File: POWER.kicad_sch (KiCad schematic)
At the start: 39 parts, among them CN1 KF128L-5.08-2P, U1 XL1509-5.0, U2 B0503S-2WR3L, U3 SY8089A1AAC, U4 CH213K, U5 SY8089AAC

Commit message: 更新PCB层叠铺铜与器件封装配置
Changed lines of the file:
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@@
 	)
 	(junction
-		(at 241.3 137.16)
+		(at 238.125 137.16)
 		(diameter 0)
 		(color 0 0 0 0)
@@
 	(wire
 		(pts
-			(xy 226.06 137.16) (xy 241.3 137.16)
+			(xy 226.06 137.16) (xy 238.125 137.16)
 		)
 		(stroke
@@
 	(wire
 		(pts
-			(xy 241.3 137.16) (xy 252.73 137.16)
+			(xy 238.125 137.16) (xy 252.73 137.16)
 		)
 		(stroke
@@
 	(symbol
 		(lib_id "power:Earth")
-		(at 241.3 137.16 0)
+		(at 238.125 137.16 0)
 		(unit 1)
 		(body_style 1)
@@
 		(fields_autoplaced yes)
 		(property "Reference" "#PWR027"
-			(at 241.3 143.51 0)
+			(at 238.125 143.51 0)
 			(hide yes)
 			(show_name no)
@@
 		)
 		(property "Value" "Earth"
-			(at 241.3 142.24 0)
+			(at 238.125 142.24 0)
 			(show_name no)
 			(do_not_autoplace no)
@@
 		)
 		(property "Footprint" ""
-			(at 241.3 137.16 0)
+			(at 238.125 137.16 0)
 			(hide yes)
 			(show_name no)
@@
 		)
 		(property "Datasheet" ""
-			(at 241.3 137.16 0)
+			(at 238.125 137.16 0)
 			(hide yes)
 			(show_name no)
@@
 		)
 		(property "Description" "Power symbol creates a global label with name \"Earth\""
-			(at 241.3 137.16 0)
+			(at 238.125 137.16 0)
 			(hide yes)
 			(show_name no)

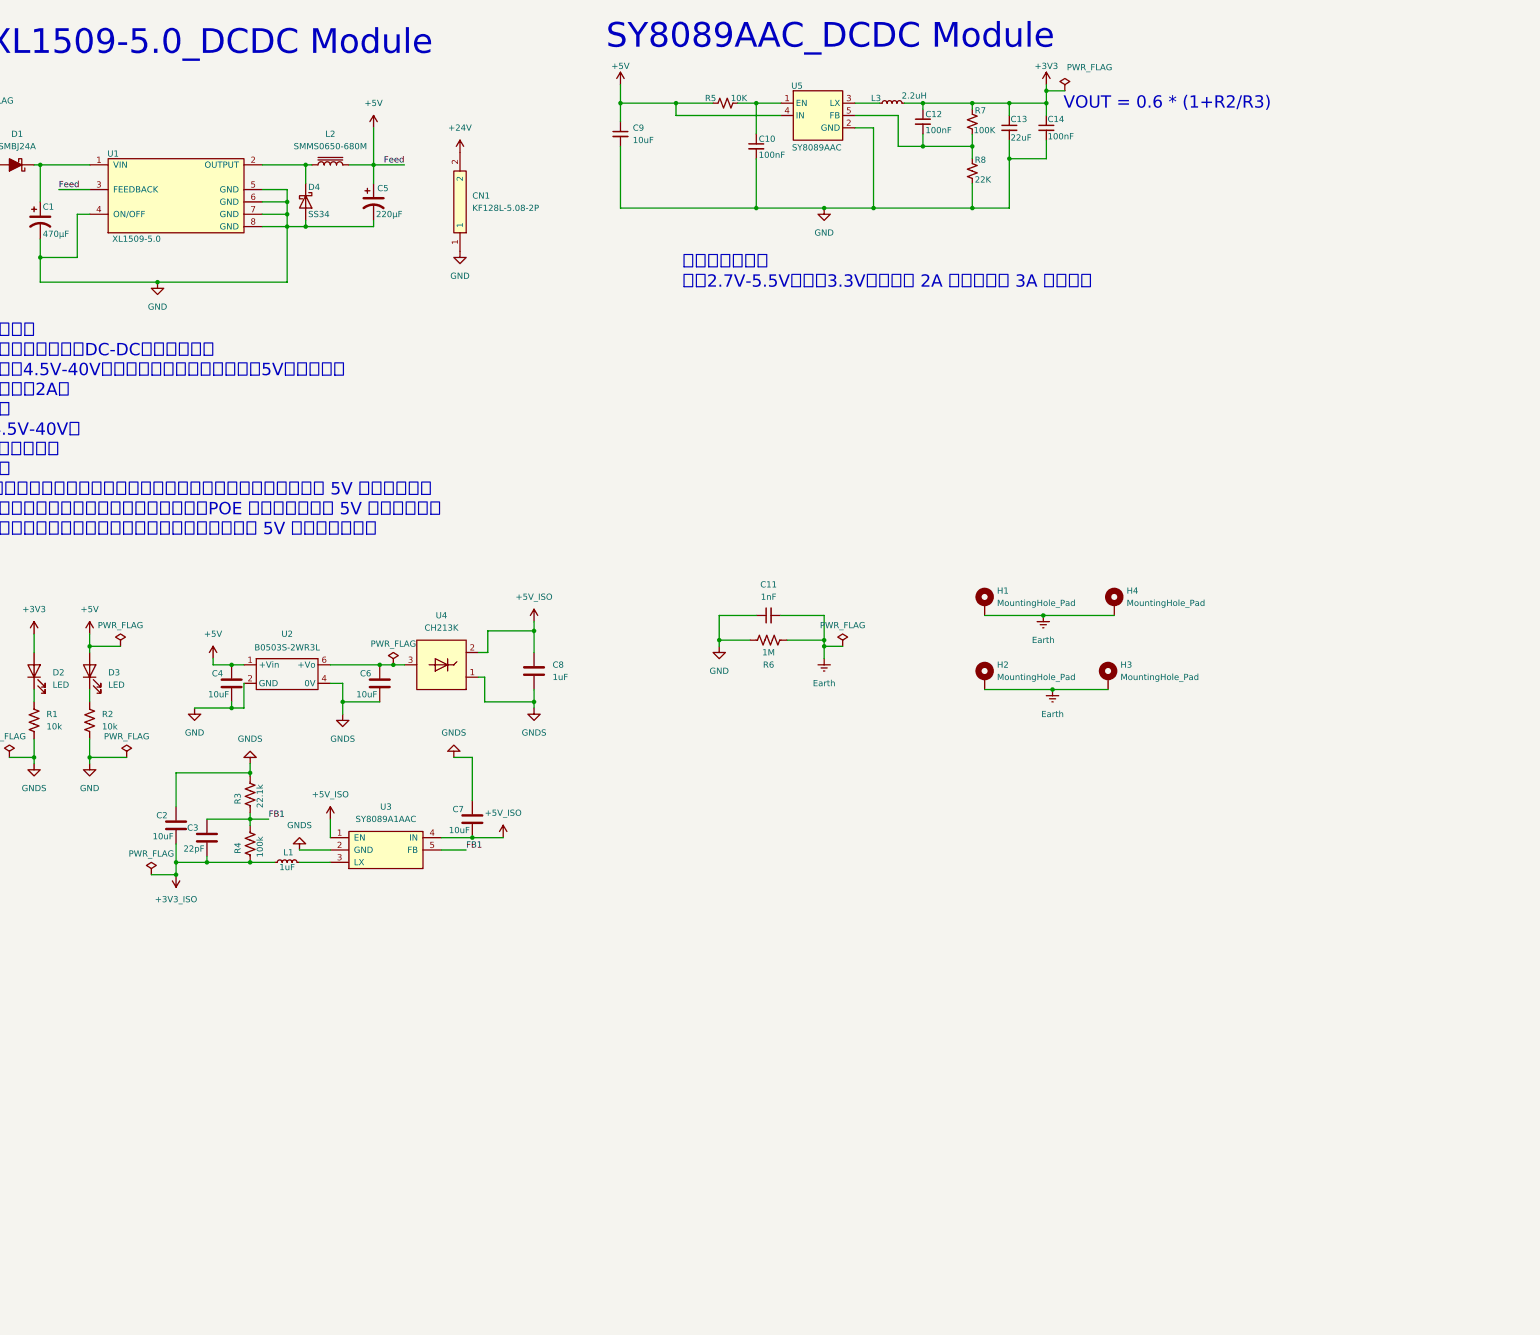
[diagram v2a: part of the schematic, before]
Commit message: 更新六层控制板设计及嘉立创生产文件
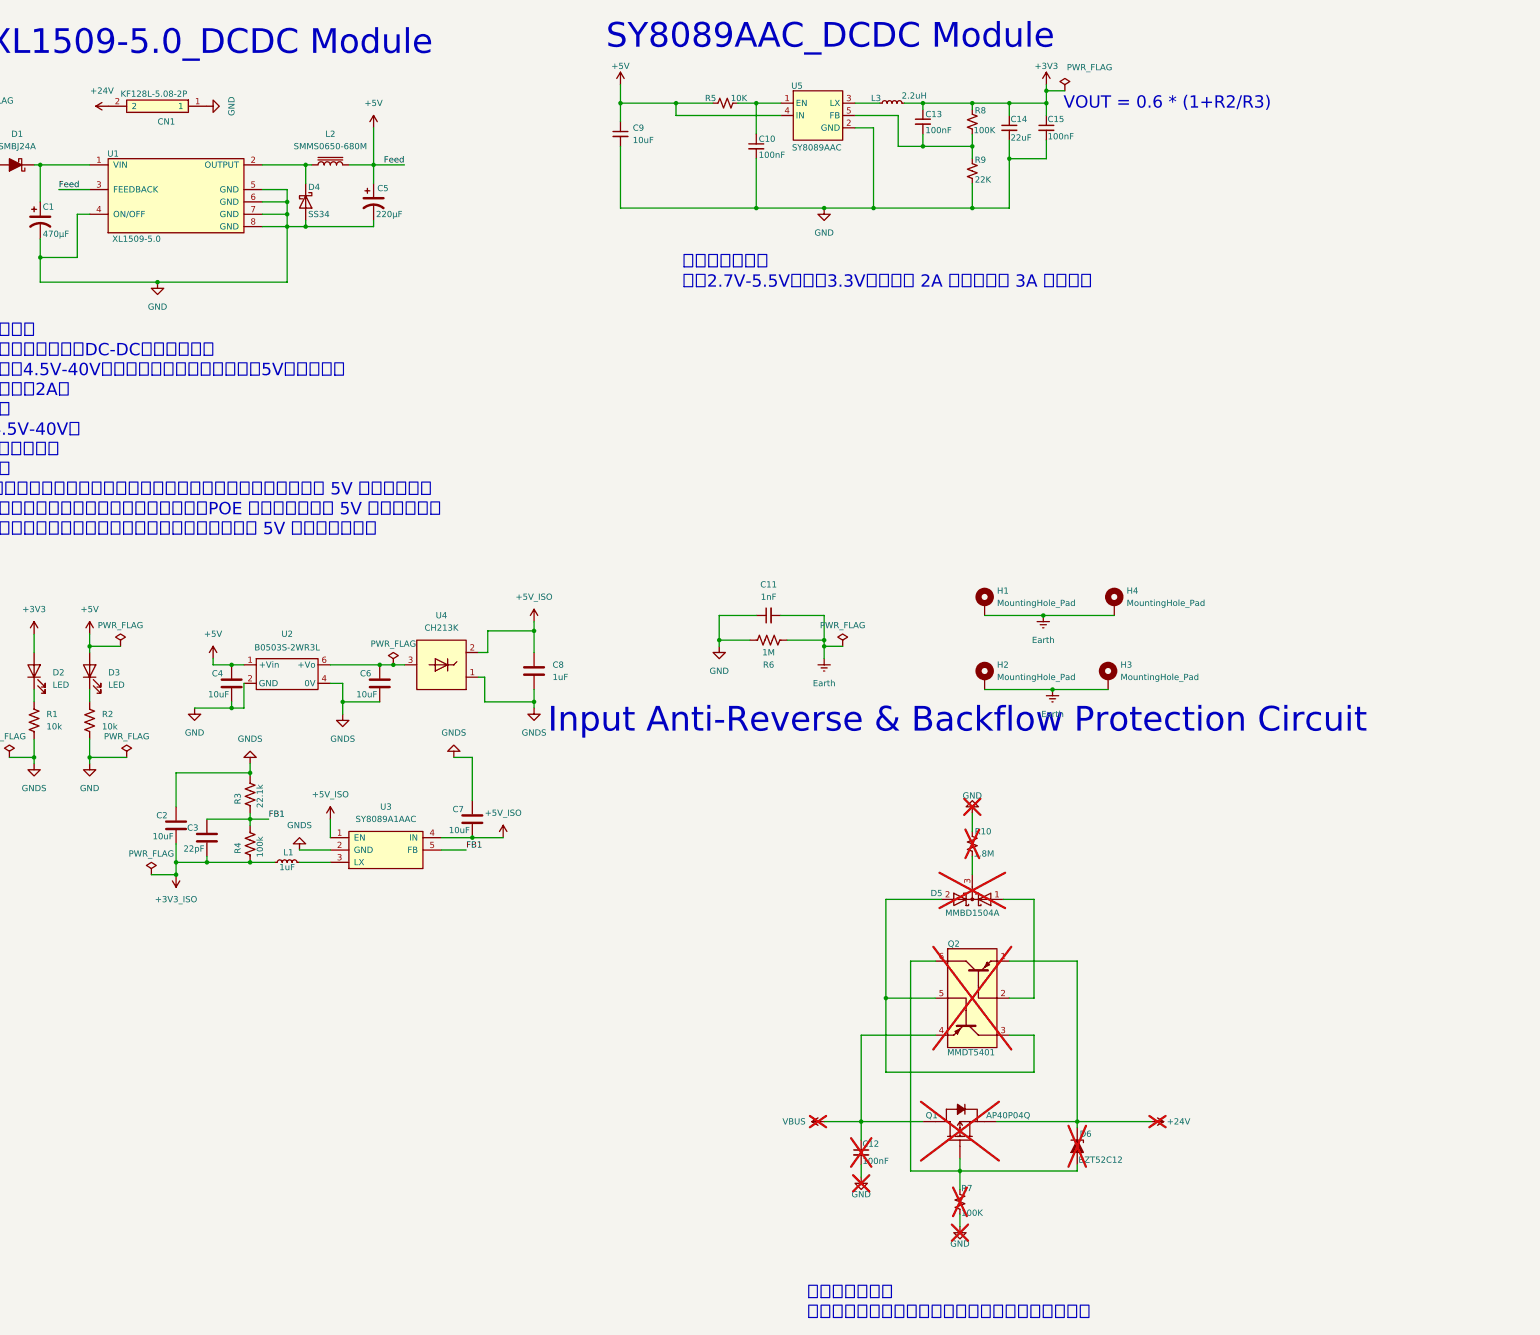
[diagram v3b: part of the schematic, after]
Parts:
- added C12: 100nF, kicad_api_lib:CC0603KRX7R9BB104, symbol CC0603KRX7R9BB104:CC0603KRX7R9BB104
- added D5: MMBD1504A, kicad_api_lib:MMBD1504A, symbol MMBD1504A:MMBD1504A
- added D6: BZT52C12, kicad_api_lib:BZT52C12, symbol BZT52C12:BZT52C12
- added Q1: AP40P04Q, kicad_api_lib:AP40P04Q, symbol AP40P04Q:AP40P04Q
- added Q2: MMDT5401, kicad_api_lib:MMDT5401, symbol MMDT5401:MMDT5401
- added R10: 1.8M, kicad_api_lib:RK73H1JTTD1804F, symbol RK73H1JTTD1804F:RK73H1JTTD1804F
- added R7: 100K, kicad_api_lib:0603WAF1003T5E, symbol 0603WAF1003T5E:0603WAF1003T5E
- renumbered C12 to C13, C13 to C14, C14 to C15, R7 to R8, R8 to R9
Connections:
- net +24V: now also D6.1 (K), Q1.1 (S), Q1.2 (S), Q1.3 (S), Q2.1 (E)
- net GND: now also C12.2, R10.1, R7.2
- new net: D5.1 (A), Q2.2 (B)
- new net: D5.2 (A), Q2.3 (C), Q2.5 (B)
- new net: D5.3 (K), R10.2
- new net: D6.2 (A), Q1.4 (G), Q2.6 (C), R7.1
- new net VBUS: C12.1, Q1.5 (D), Q1.6 (D), Q1.7 (D), Q1.8 (D), Q2.4 (E)
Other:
- note added: "Input Anti-Reverse & Backflow Protection Circuit"
- note added: "模块电路功能： 该原理图功能是对输入电源进行防反接以及过流保护"
- moved on the sheet: CN1

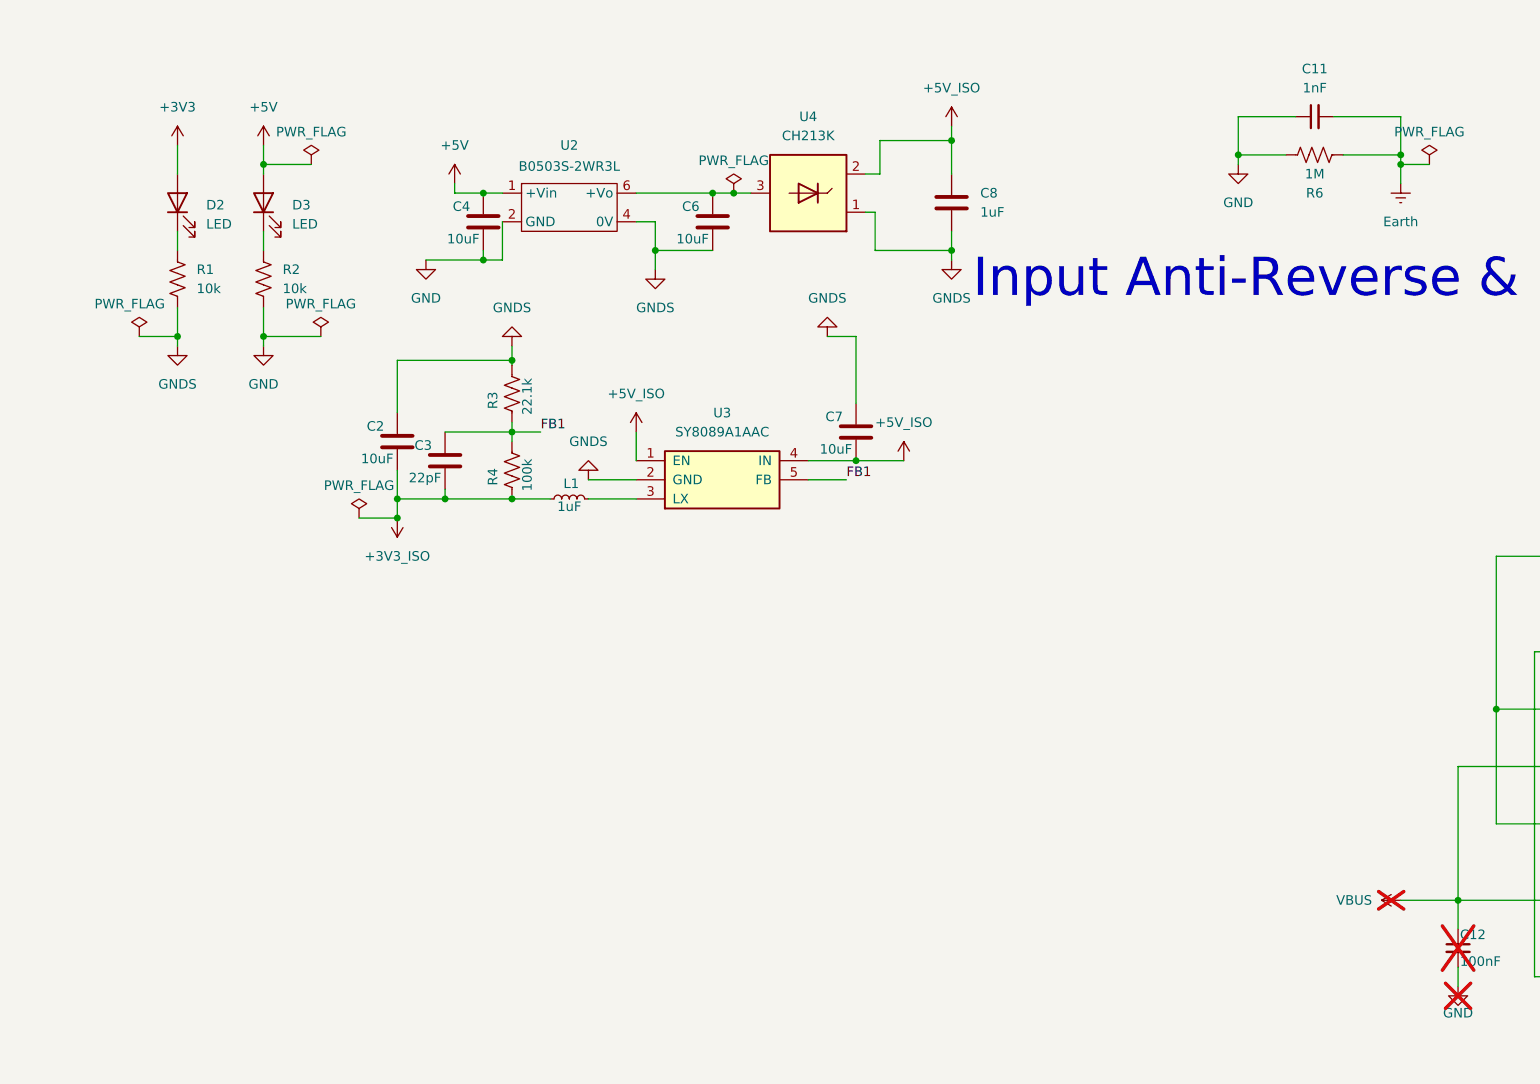
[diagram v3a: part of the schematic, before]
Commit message: 更新六层电机控制板设计与器件库
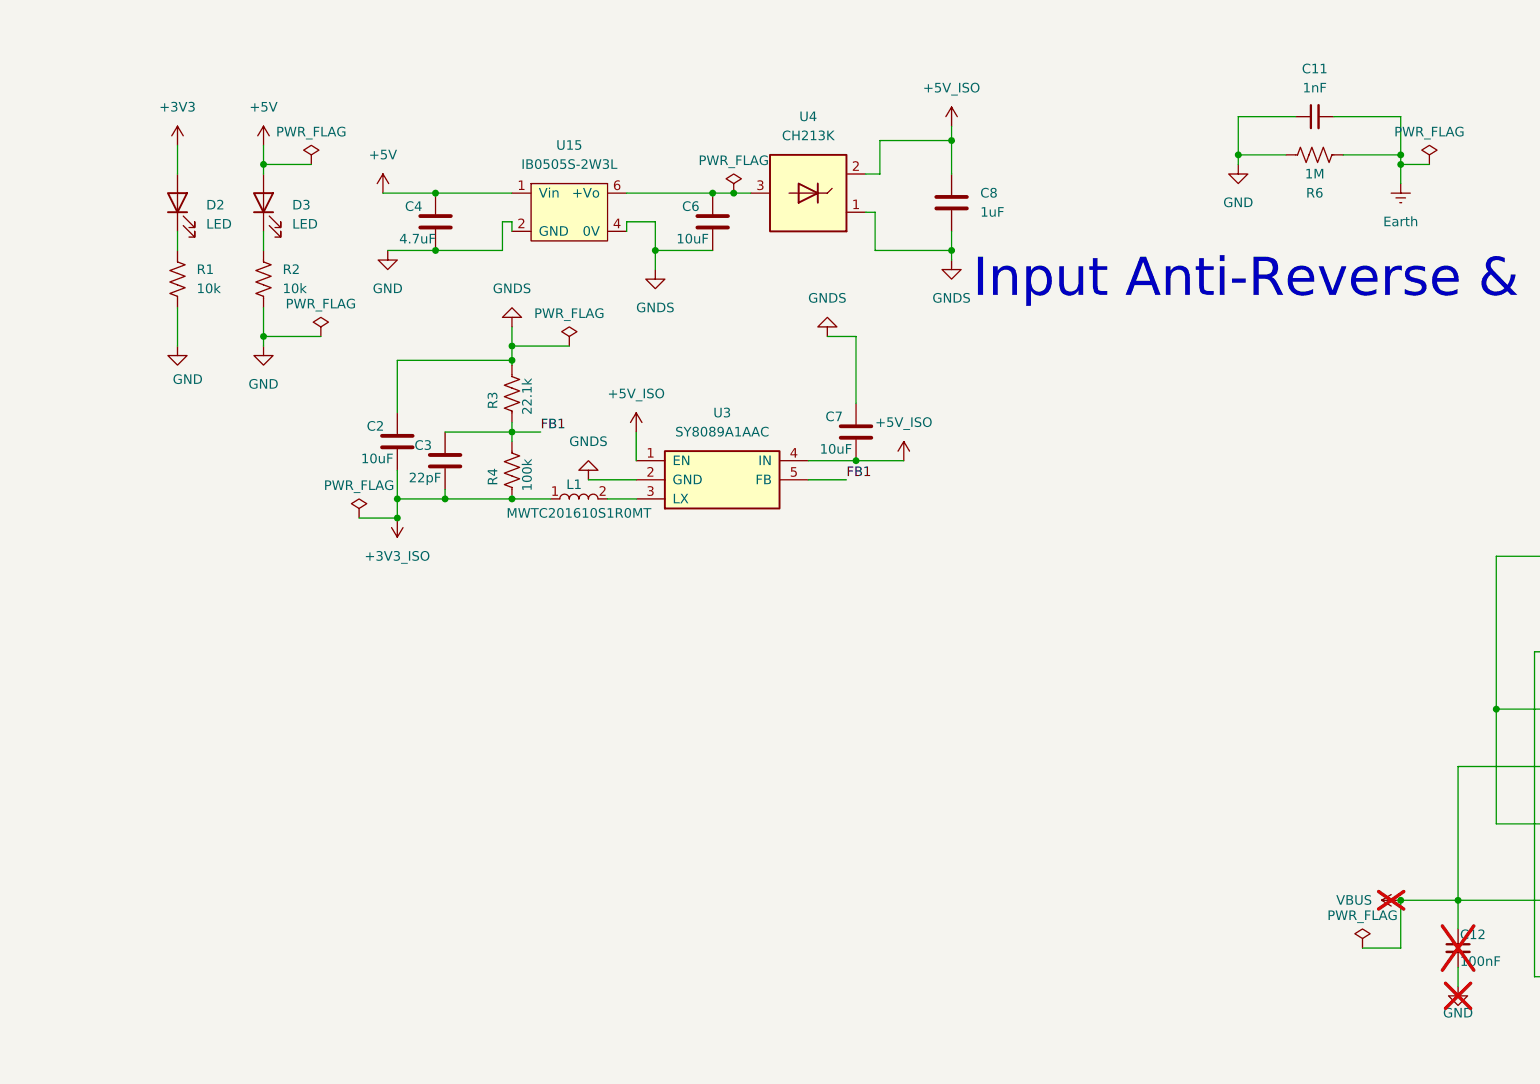
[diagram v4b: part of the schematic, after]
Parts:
- removed L1: 1uF, Capacitor_SMD:C_0603_1608Metric_Pad1.08x0.95mm_HandSolder, symbol Device:L_Small
- removed U2: B0503S-2WR3L, Converter_DCDC:B0503S-2WR3L, symbol B0503S-2WL:B0503S-2WL
- added L1: MWTC201610S1R0MT, kicad_api_lib:MWTC201610S1R0MT, symbol MWTC201610S1R0MT:L
- added U15: IB0505S-2W3L, kicad_api_lib:IB0505S-2W3L, symbol IB0505S-2W3L:IB0505S-2W3L
- C12: footprint kicad_api_lib:CC0603KRX7R9BB104 -> Capacitor_SMD:C_0603_1608Metric_Pad1.08x0.95mm_HandSolder
- C13: footprint Capacitor_SMD:C_0402_1005Metric_Pad0.74x0.62mm_HandSolder -> Capacitor_SMD:C_0603_1608Metric_Pad1.08x0.95mm_HandSolder; MFG Walsin Technologies -> Samsung Electro-Mechanics; MPN 0402B104K500CT -> CL10B104KB8NNNC; Manufacturer Walsin Technologies -> Samsung Electro-Mechanics; package 0402 -> 0603; packaging 10000pcs -> (none)
- C15: footprint Capacitor_SMD:C_0402_1005Metric_Pad0.74x0.62mm_HandSolder -> Capacitor_SMD:C_0603_1608Metric_Pad1.08x0.95mm_HandSolder
- C4: value 10uF -> 4.7uF
- D5: footprint kicad_api_lib:MMBD1504A -> Package_TO_SOT_SMD:TSOT-23_HandSoldering
- D6: footprint kicad_api_lib:BZT52C12 -> Diode_SMD:D_SOD-123
- Q2: footprint kicad_api_lib:MMDT5401 -> Package_TO_SOT_SMD:SOT-363_SC-70-6
- R10: footprint kicad_api_lib:RK73H1JTTD1804F -> Resistor_SMD:R_0603_1608Metric
- R5: footprint Resistor_SMD:R_0402_1005Metric_Pad0.72x0.64mm_HandSolder -> Resistor_SMD:R_0603_1608Metric_Pad0.98x0.95mm_HandSolder
- R7: footprint kicad_api_lib:0603WAF1003T5E -> Resistor_SMD:R_0603_1608Metric_Pad0.98x0.95mm_HandSolder
- R8, R9: footprint Resistor_SMD:R_01005_0402Metric_Pad0.57x0.30mm_HandSolder -> Resistor_SMD:R_0603_1608Metric_Pad0.98x0.95mm_HandSolder
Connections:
- net +3V3_ISO: now also L1.1
- net +5V: now also U15.1 (Vin)
- net GND: now also R1.2, U15.2 (GND)
- net GNDS: now also U15.4 (0V); no longer R1.2
- net at C6.1, U4.3 (VI+): now also U15.6 (+Vo)
- net at U3.3 (LX): now also L1.2
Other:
- moved on the sheet: C4

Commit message: 更新电源与USB供电设计、PCB及器件库
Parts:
- added C57: 4.7uF/10V, Capacitor_SMD:C_0603_1608Metric, symbol Device:C
- added C58: 1uF/10V, Capacitor_SMD:C_0603_1608Metric, symbol Device:C
- added U18: LM66100DCKR, kicad_api_lib:LM66100DCKR, symbol kicad_api_lib:LM66100DCKR
- C1: footprint Capacitor_SMD:CP_Elec_10x10.5 -> Capacitor_SMD:CP_Elec_8x10
- C5: footprint Capacitor_SMD:CP_Elec_5x5.4 -> Capacitor_SMD:CP_Elec_6.3x7.7
- renumbered C4 to C3, C3 to C4, U15 to U2
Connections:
- net +24V: now also C1.1, D1.1 (K), U1.1 (VIN); no longer D1.2 (A)
- net +5V: now also C57.1, U18.3 (CE#), U18.6 (VOUT); no longer C5.1, L2.2, U1.3 (FEEDBACK)
- net GND: now also D1.2 (A), C57.2, C58.2, U18.2 (GND), U18.5 (ST)
- new net BOARD_5V_RAW: C5.1, C58.1, L2.2, U1.3 (FEEDBACK), U18.1 (VIN)
- no-connect marks 0 -> 1
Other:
- moved on the sheet: D1
